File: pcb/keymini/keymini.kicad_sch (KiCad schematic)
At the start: 86 parts, among them J1 USB_C_Receptacle_USB2.0_16P, SW1A1 SW_Push, SW1B1 SW_Push, SW1C1 SW_Push, SW1D1 SW_Push, SW1E1 SW_Push, SW1F1 SW_Push, SW1G1 SW_Push, SW1H1 SW_Push, SW1I1 SW_Push, SW1J1 SW_Push, SW2A1 SW_Push, SW2B1 SW_Push, SW2C1 SW_Push, SW2D1 SW_Push, SW2E1 SW_Push, SW2F1 SW_Push, SW2G1 SW_Push, SW2H1 SW_Push, SW2I1 SW_Push, SW2J1 SW_Push, SW3A1 SW_Push, SW3B1 SW_Push, SW3C1 SW_Push, SW3D1 SW_Push, SW3E1 SW_Push, SW3F1 SW_Push, SW3G1 SW_Push, SW3H1 SW_Push, SW3I1 SW_Push, SW3J1 SW_Push, SW4C1 SW_Push, SW4D1 SW_Push, SW4E1 SW_Push, SW4F1 SW_Push, SW4G1 SW_Push, SW4H1 SW_Push, U1 STM32F072CBT6, U2 XC6206P332MR

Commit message: composant placement
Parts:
- removed SWB2: SW_Push, Button_Switch_SMD:SW_SPST_CK_RS282G05A3, symbol Switch:SW_Push
- renumbered SWB1 to BOOT
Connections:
- net +3.3V: now also C4.1; no longer C4.2
- net +5V: now also C1.2; no longer C1.1
- net GND: now also C1.1, C4.2, R2.1; no longer C1.2, C4.1, R2.2
- net at J1.B5 (CC2): now also R2.2; no longer R2.1
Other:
- moved on the sheet: C1, C4, R2
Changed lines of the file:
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@@
 	(paper "A4")
 	(junction
-		(at 21.59 180.34)
+		(at 170.18 160.02)
 		(diameter 0)
 		(color 0 0 0 0)
@@
 	)
 	(junction
-		(at 170.18 160.02)
+		(at 81.28 180.34)
 		(diameter 0)
 		(color 0 0 0 0)
@@
 	)
 	(junction
-		(at 81.28 180.34)
-		(diameter 0)
-		(color 0 0 0 0)
-	)
-	(junction
-		(at 81.28 187.96)
-		(diameter 0)
-		(color 0 0 0 0)
-	)
-	(junction
 		(at 116.84 100.33)
 		(diameter 0)
@@
 	)
 	(junction
-		(at 218.44 38.1)
-		(diameter 0)
-		(color 0 0 0 0)
-	)
-	(junction
 		(at 259.08 27.94)
 		(diameter 0)
@@
 	)
 	(junction
-		(at 208.28 38.1)
+		(at 21.59 180.34)
+		(diameter 0)
+		(color 0 0 0 0)
+	)
+	(junction
+		(at 81.28 187.96)
 		(diameter 0)
 		(color 0 0 0 0)
@@
 	(wire
 		(pts
-			(xy 81.28 187.96) (xy 95.25 187.96)
-		)
-		(stroke
-			(width 0)
-			(type default)
-		)
-	)
-	(wire
-		(pts
 			(xy 95.25 180.34) (xy 109.22 180.34)
 		)
@@
 	(wire
 		(pts
-			(xy 41.91 114.3) (xy 41.91 128.27)
+			(xy 81.28 187.96) (xy 95.25 187.96)
 		)
 		(stroke
@@
 	(wire
 		(pts
-			(xy 254 27.94) (xy 256.54 27.94)
+			(xy 41.91 114.3) (xy 41.91 128.27)
 		)
 		(stroke
@@
 	(wire
 		(pts
-			(xy 256.54 27.94) (xy 259.08 27.94)
+			(xy 254 27.94) (xy 256.54 27.94)
 		)
 		(stroke
@@
 	(wire
 		(pts
-			(xy 226.06 38.1) (xy 238.76 38.1)
+			(xy 256.54 27.94) (xy 259.08 27.94)
 		)
 		(stroke
@@
 	(wire
 		(pts
-			(xy 208.28 38.1) (xy 208.28 50.8)
+			(xy 226.06 38.1) (xy 238.76 38.1)
 		)
 		(stroke
@@
 	(wire
 		(pts
-			(xy 218.44 38.1) (xy 218.44 50.8)
-		)
-		(stroke
-			(width 0)
-			(type default)
-		)
-	)
-	(wire
-		(pts
 			(xy 153.67 24.13) (xy 153.67 38.1)
 		)
@@
 	(symbol
 		(lib_id "Device:C")
-		(at 21.59 184.15 0)
+		(at 21.59 184.15 180)
 		(unit 1)
 		(exclude_from_sim no)
@@
 					(size 1.27 1.27)
 				)
-				(justify left)
+				(justify right)
 			)
 		)
@@
 					(size 1.27 1.27)
 				)
-				(justify left)
+				(justify right)
 			)
 		)
 		(property "Footprint" "Capacitor_SMD:C_0805_2012Metric"
-			(at 22.5552 187.96 0)
+			(at 20.6248 180.34 0)
 			(effects
 				(font
@@
 	(symbol
 		(lib_id "Device:C")
-		(at 81.28 184.15 180)
+		(at 81.28 184.15 0)
 		(unit 1)
 		(exclude_from_sim no)
@@
 					(size 1.27 1.27)
 				)
-				(justify right)
+				(justify left)
 			)
 		)
@@
 					(size 1.27 1.27)
 				)
-				(justify right)
+				(justify left)
 			)
 		)
 		(property "Footprint" "Capacitor_SMD:C_0805_2012Metric"
-			(at 80.3148 180.34 0)
+			(at 82.2452 187.96 0)
 			(effects
 				(font
@@
 		(dnp no)
 		(fields_autoplaced yes)
-		(property "Reference" "SWB1"
+		(property "Reference" "BOOT"
 			(at 213.36 30.48 0)
 			(effects
@@
 			(project ""
 				(path "/5ef0dab6-ab05-4045-8a8e-70c16fe91fb0"
-					(reference "SWB1")
+					(reference "BOOT")
 					(unit 1)
 				)
@@
 	(symbol
 		(lib_id "Device:R")
-		(at 166.37 160.02 90)
+		(at 166.37 160.02 270)
 		(unit 1)
 		(exclude_from_sim no)
@@
 		)
 		(property "Footprint" "Resistor_SMD:R_0805_2012Metric"
-			(at 166.37 161.798 90)
+			(at 166.37 158.242 90)
 			(effects
 				(font
@@
 					(unit 1)
 				)
-			)
-		)
-	)
-	(symbol
-		(lib_id "Switch:SW_Push")
-		(at 213.36 50.8 0)
-		(unit 1)
-		(exclude_from_sim no)
-		(in_bom yes)
-		(on_board yes)
-		(dnp no)
-		(fields_autoplaced yes)
-		(property "Reference" "SWB2"
-			(at 213.36 43.18 0)
-			(effects
-				(font
-					(size 1.27 1.27)
-				)
-			)
-		)
-		(property "Value" "SW_Push"
-			(at 213.36 45.72 0)
-			(effects
-				(font
-					(size 1.27 1.27)
-				)
-			)
-		)
-		(property "Footprint" "Button_Switch_SMD:SW_SPST_CK_RS282G05A3"
-			(at 213.36 45.72 0)
-			(effects
-				(font
-					(size 1.27 1.27)
-				)
-				(hide yes)
-			)
-		)
-		(property "Datasheet" "~"
-			(at 213.36 45.72 0)
-			(effects
-				(font
-					(size 1.27 1.27)
-				)
-				(hide yes)
-			)
-		)
-		(property "Description" "Push button switch, generic, two pins"
-			(at 213.36 50.8 0)
-			(effects
-				(font
-					(size 1.27 1.27)
-				)
-				(hide yes)
-			)
-		)
-		(pin "1"
-		)
-		(pin "2"
-		)
-		(instances
-			(project "keymini"
-				(path "/5ef0dab6-ab05-4045-8a8e-70c16fe91fb0"
-					(reference "SWB2")
-					(unit 1)
-				)

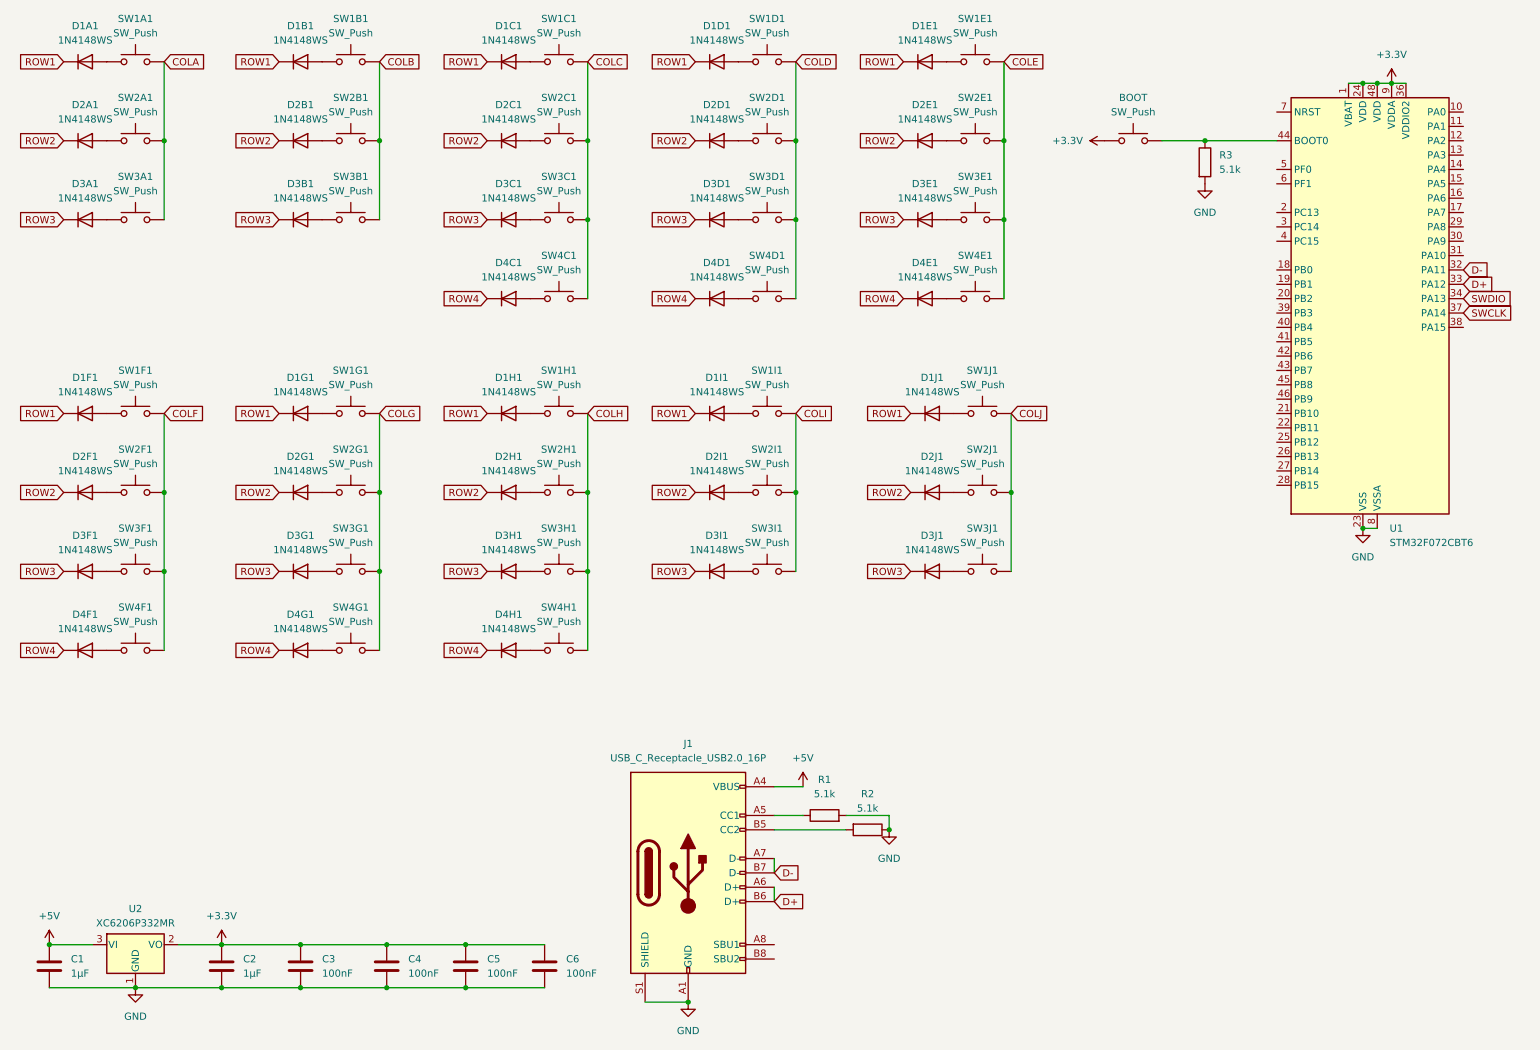
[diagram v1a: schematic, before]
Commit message: rename switches and diodes
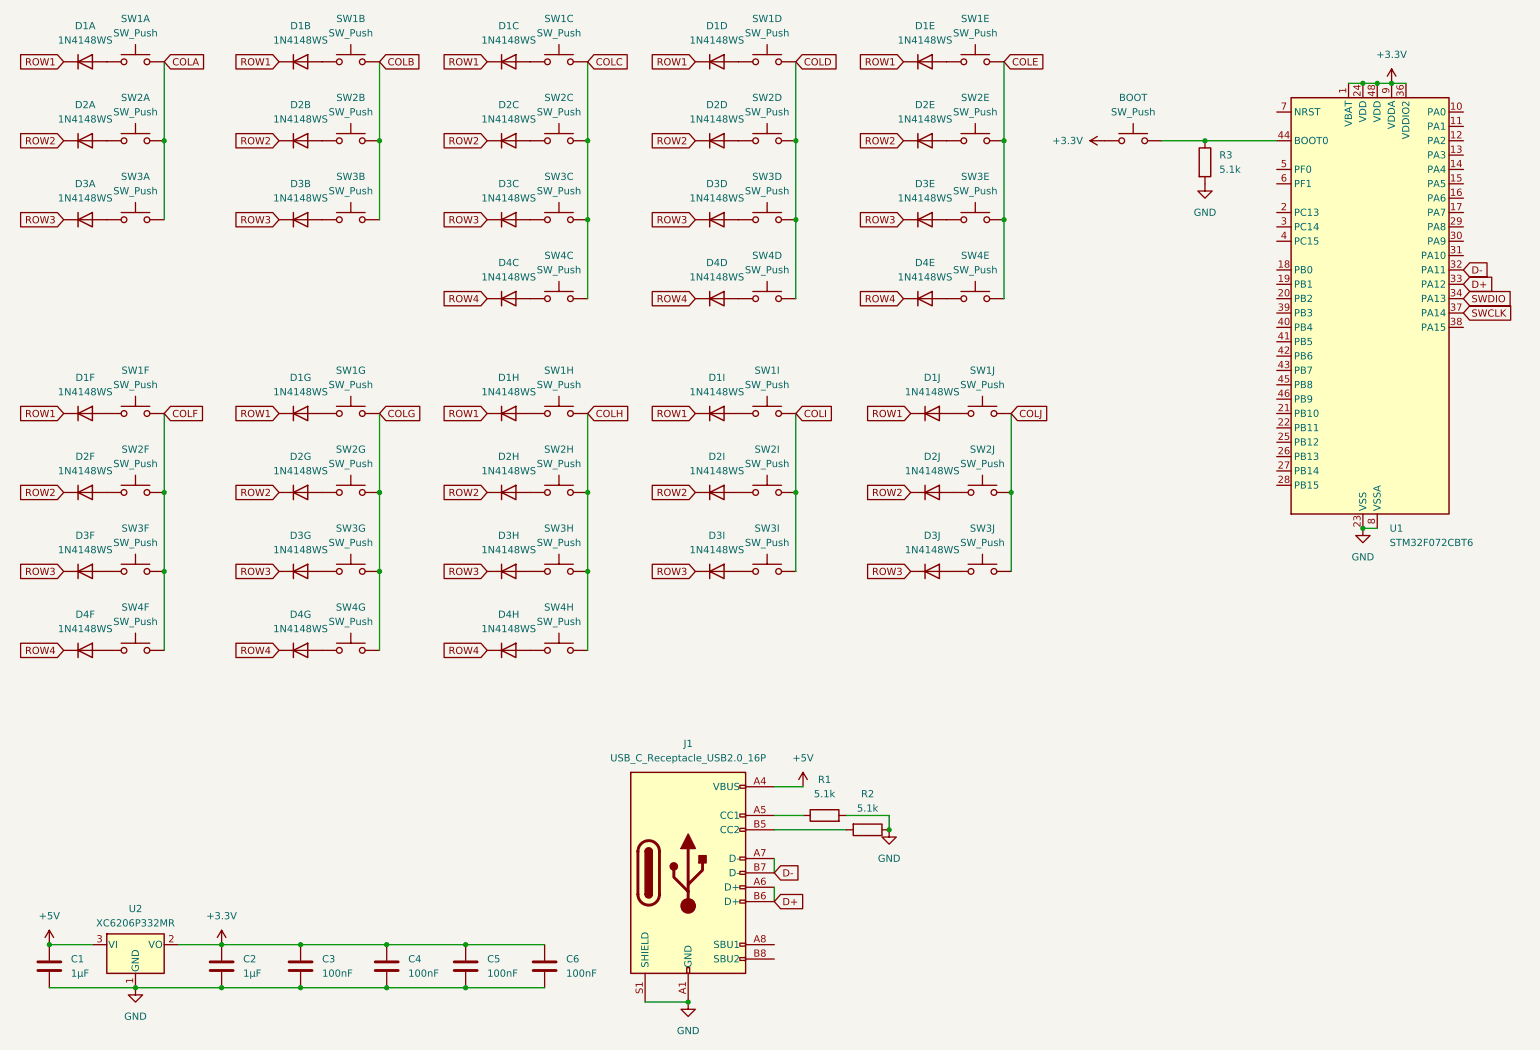
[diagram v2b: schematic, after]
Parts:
- renumbered D1A1 to D1A, D1B1 to D1B, D1C1 to D1C, D1D1 to D1D, D1E1 to D1E, D1F1 to D1F, D1G1 to D1G, D1H1 to D1H, D1I1 to D1I, D1J1 to D1J, D2A1 to D2A, D2B1 to D2B, D2C1 to D2C, D2D1 to D2D, D2E1 to D2E, D2F1 to D2F, D2G1 to D2G, D2H1 to D2H, D2I1 to D2I, D2J1 to D2J, D3A1 to D3A, D3B1 to D3B, D3C1 to D3C, D3D1 to D3D, D3E1 to D3E, D3F1 to D3F, D3G1 to D3G, D3H1 to D3H, D3I1 to D3I, D3J1 to D3J, D4C1 to D4C, D4D1 to D4D, D4E1 to D4E, D4F1 to D4F, D4G1 to D4G, D4H1 to D4H, SW1A1 to SW1A, SW1B1 to SW1B, SW1C1 to SW1C, SW1D1 to SW1D, SW1E1 to SW1E, SW1F1 to SW1F, SW1G1 to SW1G, SW1H1 to SW1H, SW1I1 to SW1I, SW1J1 to SW1J, SW2A1 to SW2A, SW2B1 to SW2B, SW2C1 to SW2C, SW2D1 to SW2D, SW2E1 to SW2E, SW2F1 to SW2F, SW2G1 to SW2G, SW2H1 to SW2H, SW2I1 to SW2I, SW2J1 to SW2J, SW3A1 to SW3A, SW3B1 to SW3B, SW3C1 to SW3C, SW3D1 to SW3D, SW3E1 to SW3E, SW3F1 to SW3F, SW3G1 to SW3G, SW3H1 to SW3H, SW3I1 to SW3I, SW3J1 to SW3J, SW4C1 to SW4C, SW4D1 to SW4D, SW4E1 to SW4E, SW4F1 to SW4F, SW4G1 to SW4G, SW4H1 to SW4H

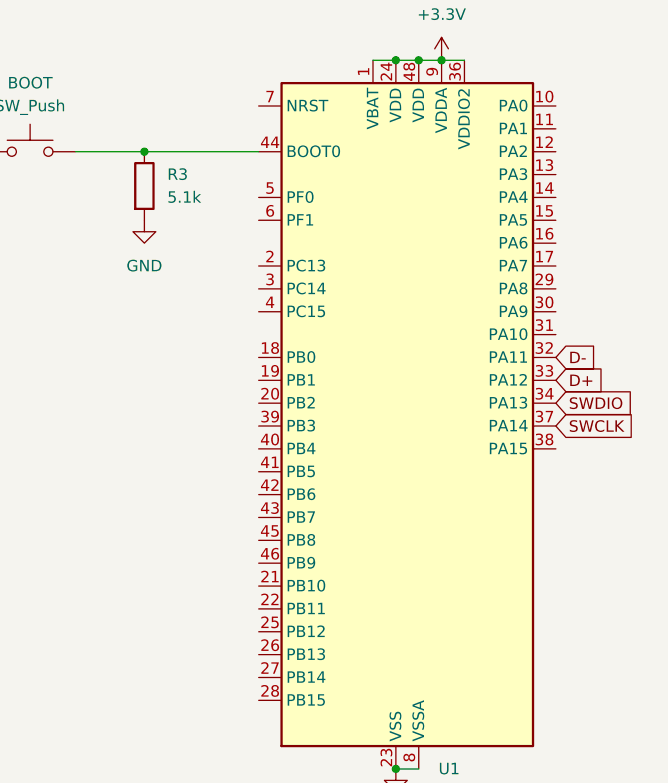
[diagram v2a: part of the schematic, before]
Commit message: rows and cols connected
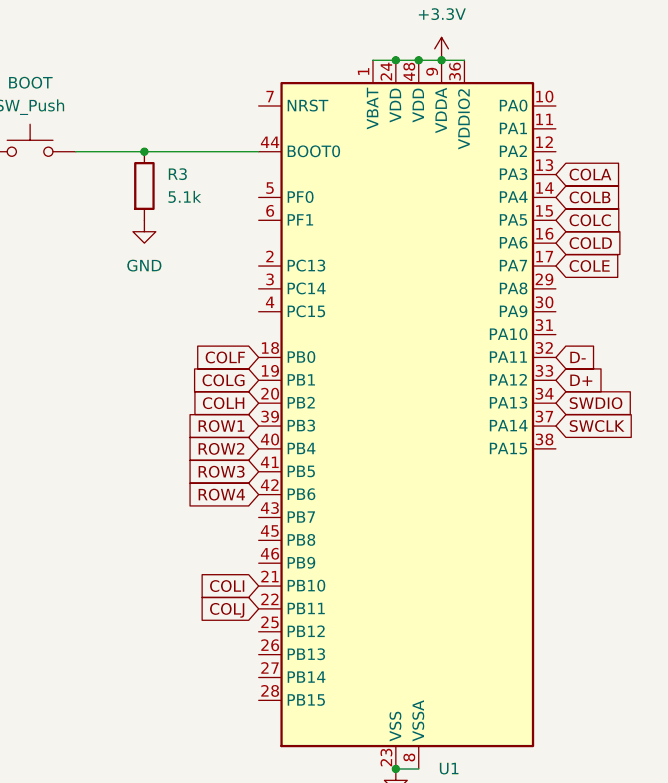
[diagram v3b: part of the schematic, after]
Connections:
- net COLA: now also U1.13 (PA3)
- net COLB: now also U1.14 (PA4)
- net COLC: now also U1.15 (PA5)
- net COLD: now also U1.16 (PA6)
- net COLE: now also U1.17 (PA7)
- net COLF: now also U1.18 (PB0)
- net COLG: now also U1.19 (PB1)
- net COLH: now also U1.20 (PB2)
- net COLI: now also U1.21 (PB10)
- net COLJ: now also U1.22 (PB11)
- net ROW1: now also U1.39 (PB3)
- net ROW2: now also U1.40 (PB4)
- net ROW3: now also U1.41 (PB5)
- net ROW4: now also U1.42 (PB6)

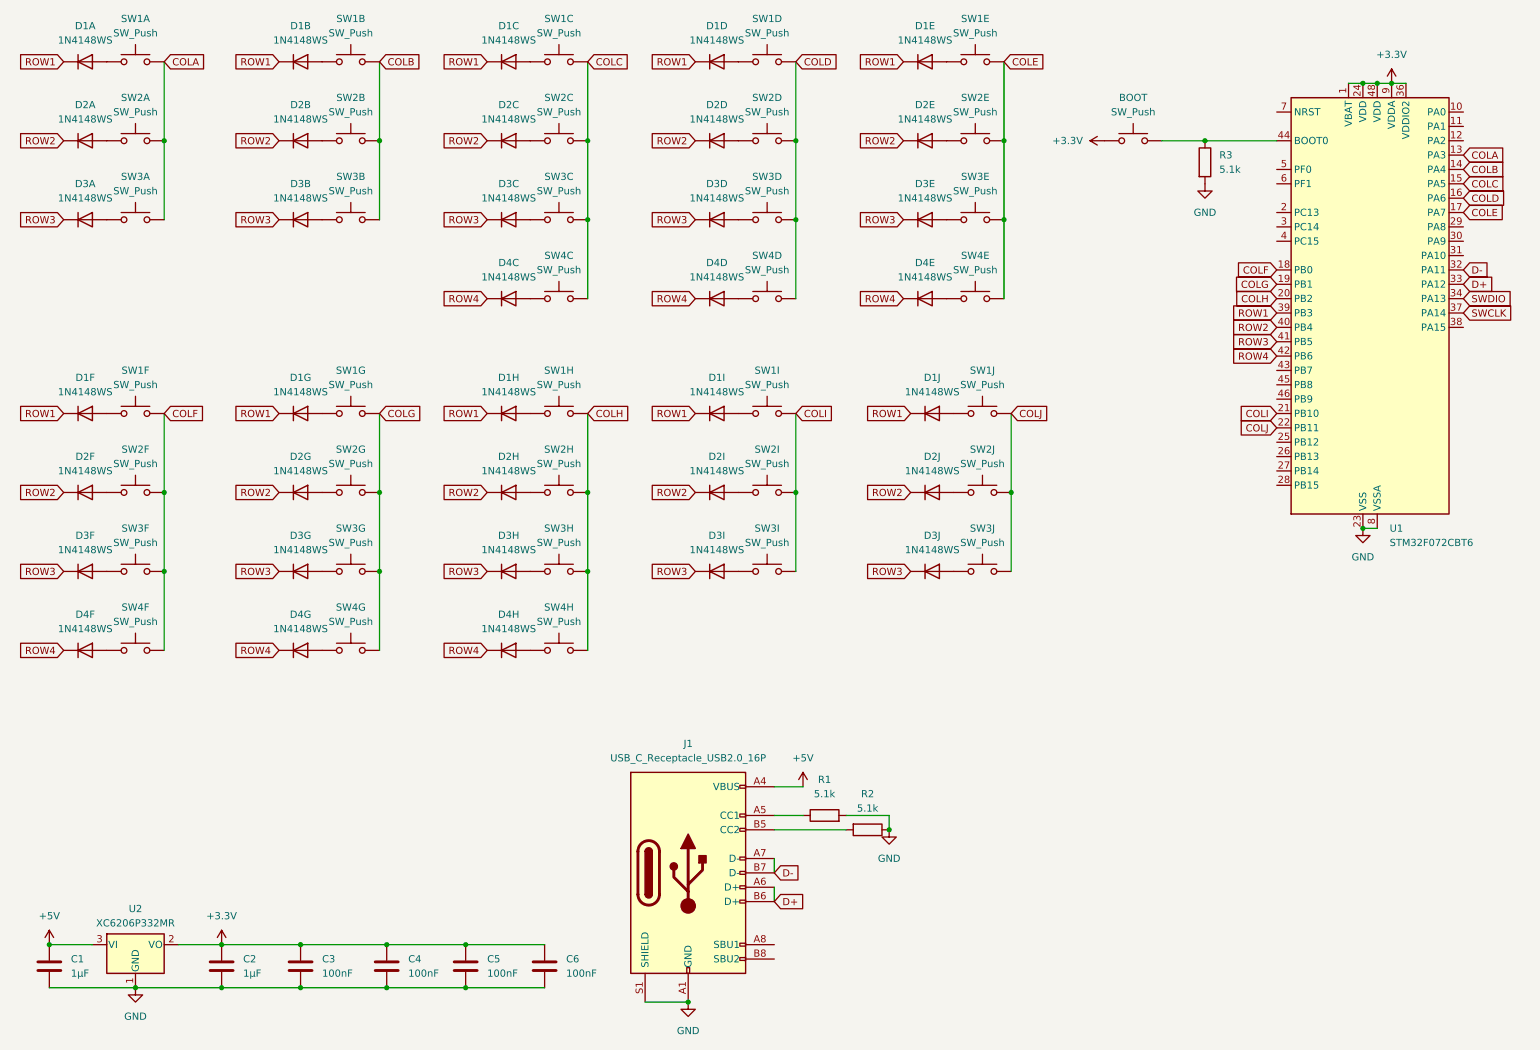
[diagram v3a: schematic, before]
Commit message: Add SWD connector
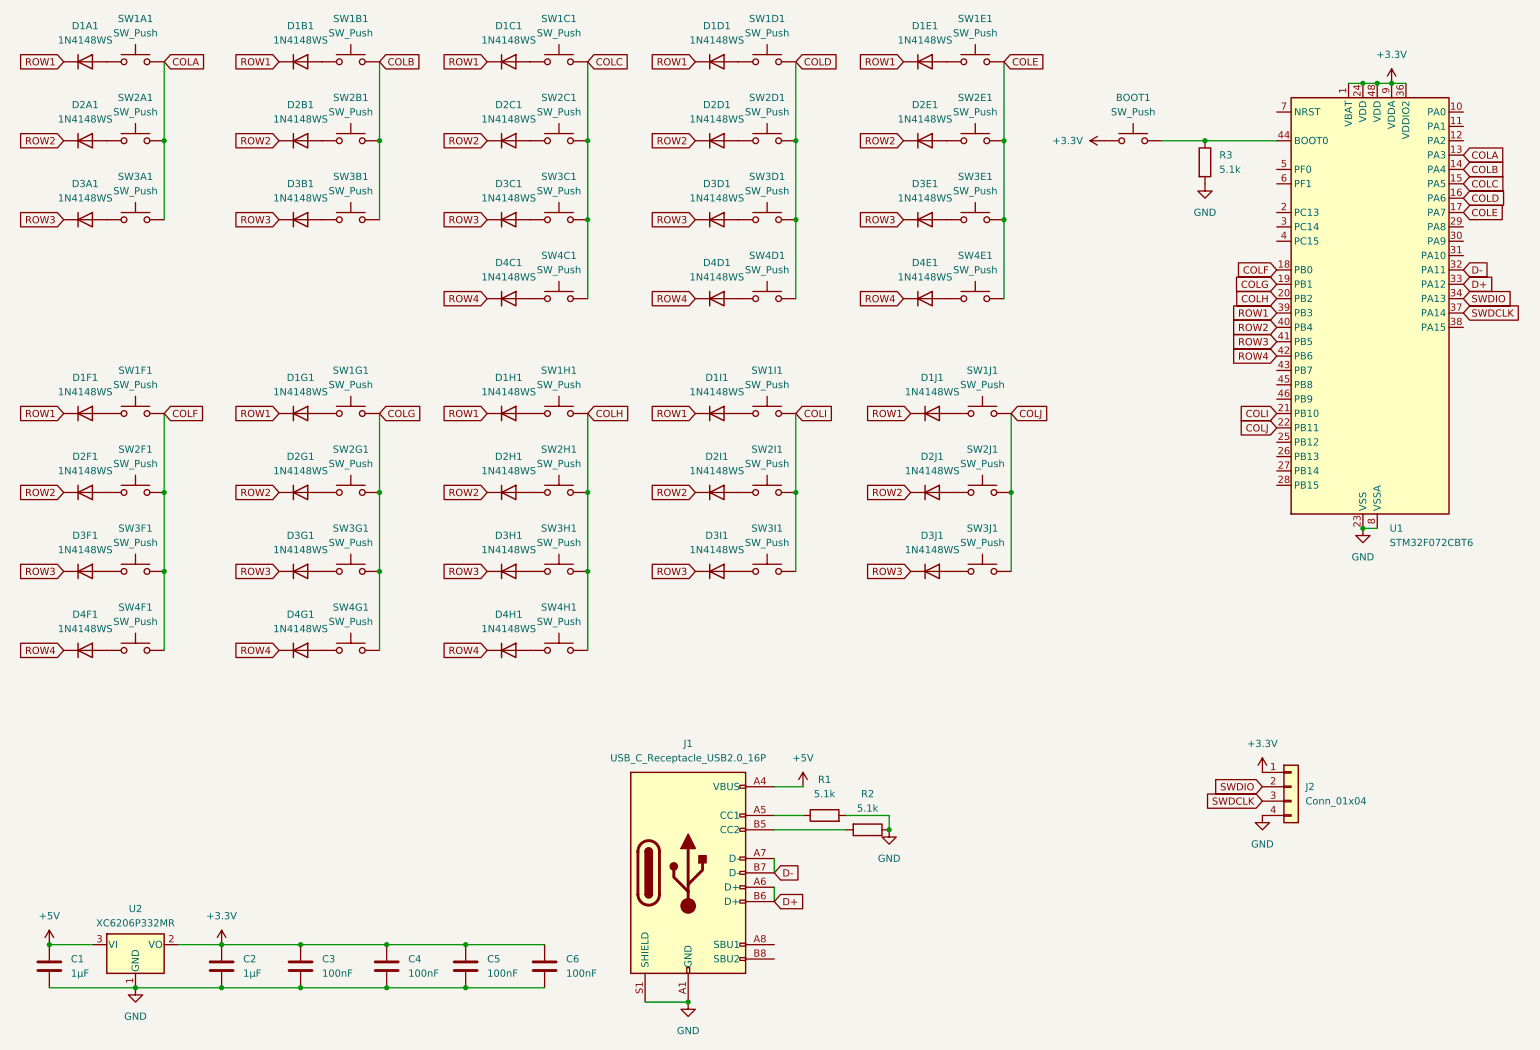
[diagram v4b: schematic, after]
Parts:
- added J2: Conn_01x04, Connector_Harwin:Harwin_M20-89004xx_1x04_P2.54mm_Horizontal, symbol Connector_Generic:Conn_01x04
- renumbered BOOT to BOOT1, D1A to D1A1, D1B to D1B1, D1C to D1C1, D1D to D1D1, D1E to D1E1, D1F to D1F1, D1G to D1G1, D1H to D1H1, D1I to D1I1, D1J to D1J1, D2A to D2A1, D2B to D2B1, D2C to D2C1, D2D to D2D1, D2E to D2E1, D2F to D2F1, D2G to D2G1, D2H to D2H1, D2I to D2I1, D2J to D2J1, D3A to D3A1, D3B to D3B1, D3C to D3C1, D3D to D3D1, D3E to D3E1, D3F to D3F1, D3G to D3G1, D3H to D3H1, D3I to D3I1, D3J to D3J1, D4C to D4C1, D4D to D4D1, D4E to D4E1, D4F to D4F1, D4G to D4G1, D4H to D4H1, SW1A to SW1A1, SW1B to SW1B1, SW1C to SW1C1, SW1D to SW1D1, SW1E to SW1E1, SW1F to SW1F1, SW1G to SW1G1, SW1H to SW1H1, SW1I to SW1I1, SW1J to SW1J1, SW2A to SW2A1, SW2B to SW2B1, SW2C to SW2C1, SW2D to SW2D1, SW2E to SW2E1, SW2F to SW2F1, SW2G to SW2G1, SW2H to SW2H1, SW2I to SW2I1, SW2J to SW2J1, SW3A to SW3A1, SW3B to SW3B1, SW3C to SW3C1, SW3D to SW3D1, SW3E to SW3E1, SW3F to SW3F1, SW3G to SW3G1, SW3H to SW3H1, SW3I to SW3I1, SW3J to SW3J1, SW4C to SW4C1, SW4D to SW4D1, SW4E to SW4E1, SW4F to SW4F1, SW4G to SW4G1, SW4H to SW4H1
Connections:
- net +3.3V: now also J2.1 (Pin_1)
- net GND: now also J2.4 (Pin_4)
- net SWDIO: now also J2.2 (Pin_2)
- net SWCLK renamed SWDCLK
- net SWDCLK: now also J2.3 (Pin_3)
